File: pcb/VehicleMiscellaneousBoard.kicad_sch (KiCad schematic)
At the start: 4 parts, among them J1 Conn_02x05_Top_Bottom, U1 OpenMV H7+, U2 Seeed_Studio_XIAO-ESP32-S3-Se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

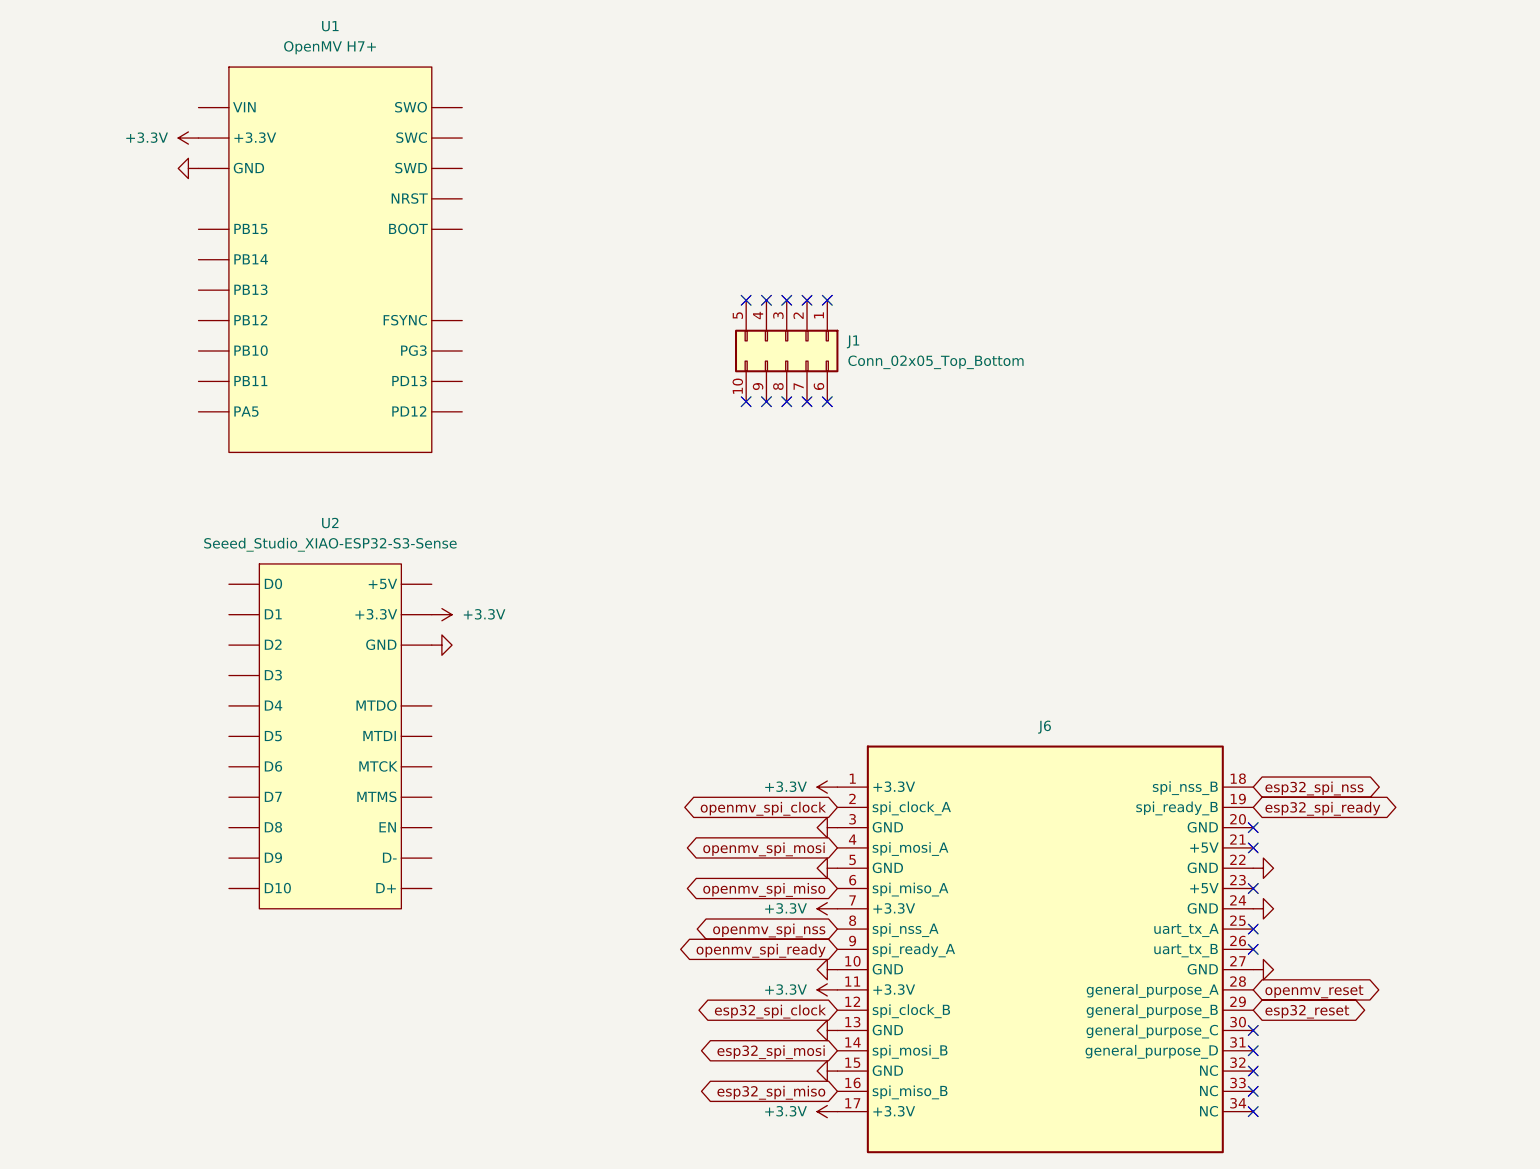
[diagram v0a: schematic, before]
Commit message: Routed `VehicleMiscellaneousBoard`.
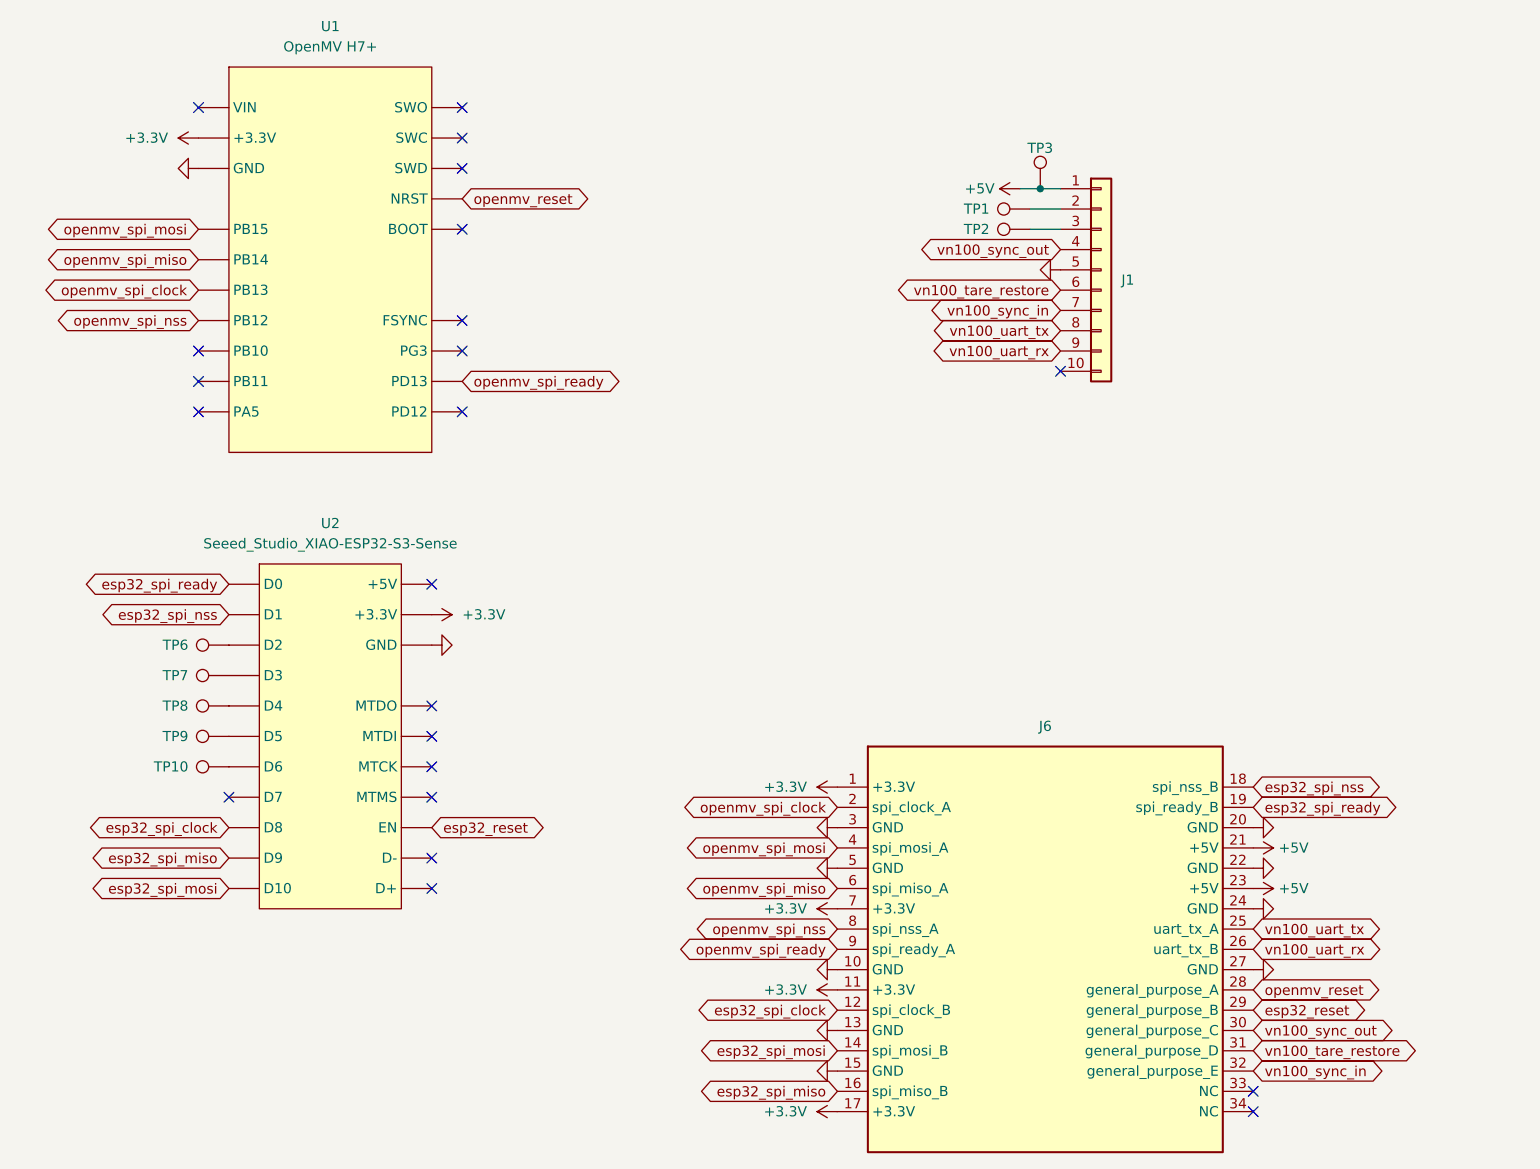
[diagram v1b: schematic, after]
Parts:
- added TP1, TP10, TP2, TP3, TP6, TP7, TP8, TP9: TestPoint, TestPoint:TestPoint_Pad_1.0x1.0mm, symbol Connector:TestPoint
- J1: symbol Connector_Generic:Conn_02x05_Top_Bottom -> Connector_Generic:Conn_01x10
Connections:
- net GND: now also J1.5 (Pin_5), J6.20 (GND)
- net esp32_reset: now also U2.EN
- net esp32_spi_clock: now also U2.D8
- net esp32_spi_miso: now also U2.D9
- net esp32_spi_mosi: now also U2.D10
- net esp32_spi_nss: now also U2.D1
- net esp32_spi_ready: now also U2.D0
- net openmv_reset: now also U1.NRST
- net openmv_spi_clock: now also U1.PB13
- net openmv_spi_miso: now also U1.PB14
- net openmv_spi_mosi: now also U1.PB15
- net openmv_spi_nss: now also U1.PB12
- net openmv_spi_ready: now also U1.PD13
- net +5V: now reaches J6.21 (+5V)
- net +5V: now also J1.1 (Pin_1), J6.23 (+5V), TP3.1
- net vn100_uart_tx: now reaches J6.25 (uart_tx_A)
- net vn100_uart_tx: now also J1.8 (Pin_8)
- net vn100_uart_rx: now reaches J6.26 (uart_tx_B)
- net vn100_uart_rx: now also J1.9 (Pin_9)
- net vn100_sync_out: now reaches J6.30 (general_purpose_C)
- net vn100_sync_out: now also J1.4 (Pin_4)
- net vn100_tare_restore: now reaches J6.31 (general_purpose_D)
- net vn100_tare_restore: now also J1.6 (Pin_6)
- net vn100_sync_in: now reaches J6.32 (general_purpose_E)
- net vn100_sync_in: now also J1.7 (Pin_7)
- net at U2.D2: now also TP6.1
- net at U2.D3: now also TP7.1
- net at U2.D4: now also TP8.1
- net at U2.D5: now also TP9.1
- net at U2.D6: now also TP10.1
- net at J1.2 (Pin_2): now also TP1.1
- net at J1.3 (Pin_3): now also TP2.1
- no-connect marks 20 -> 22
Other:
- moved on the sheet: J1

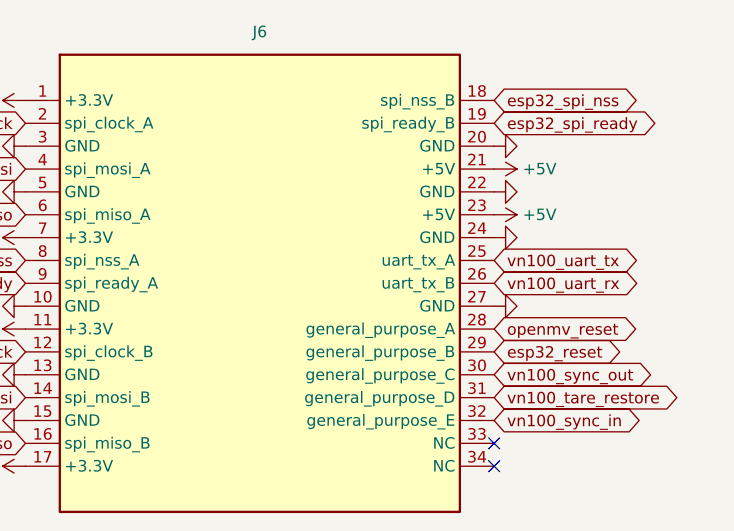
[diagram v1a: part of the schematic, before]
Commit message: Fixed inconsistency of `VehicleStackConnector` in `VehicleFlightComputer` and `VehicleMiscellaneousBoard`.
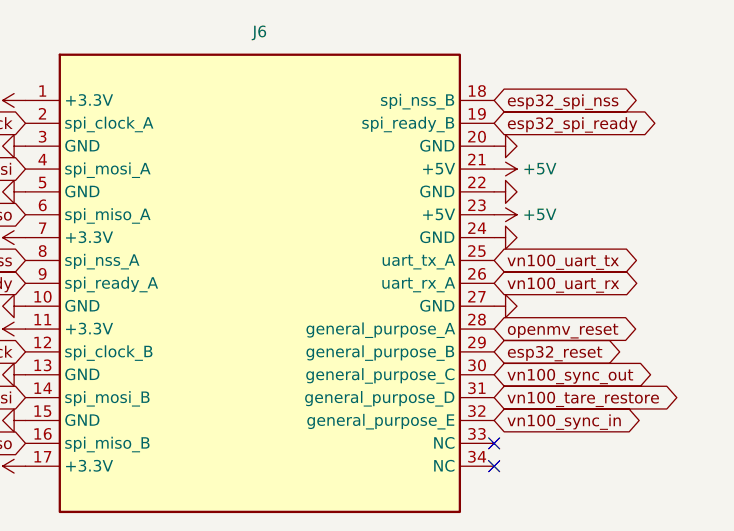
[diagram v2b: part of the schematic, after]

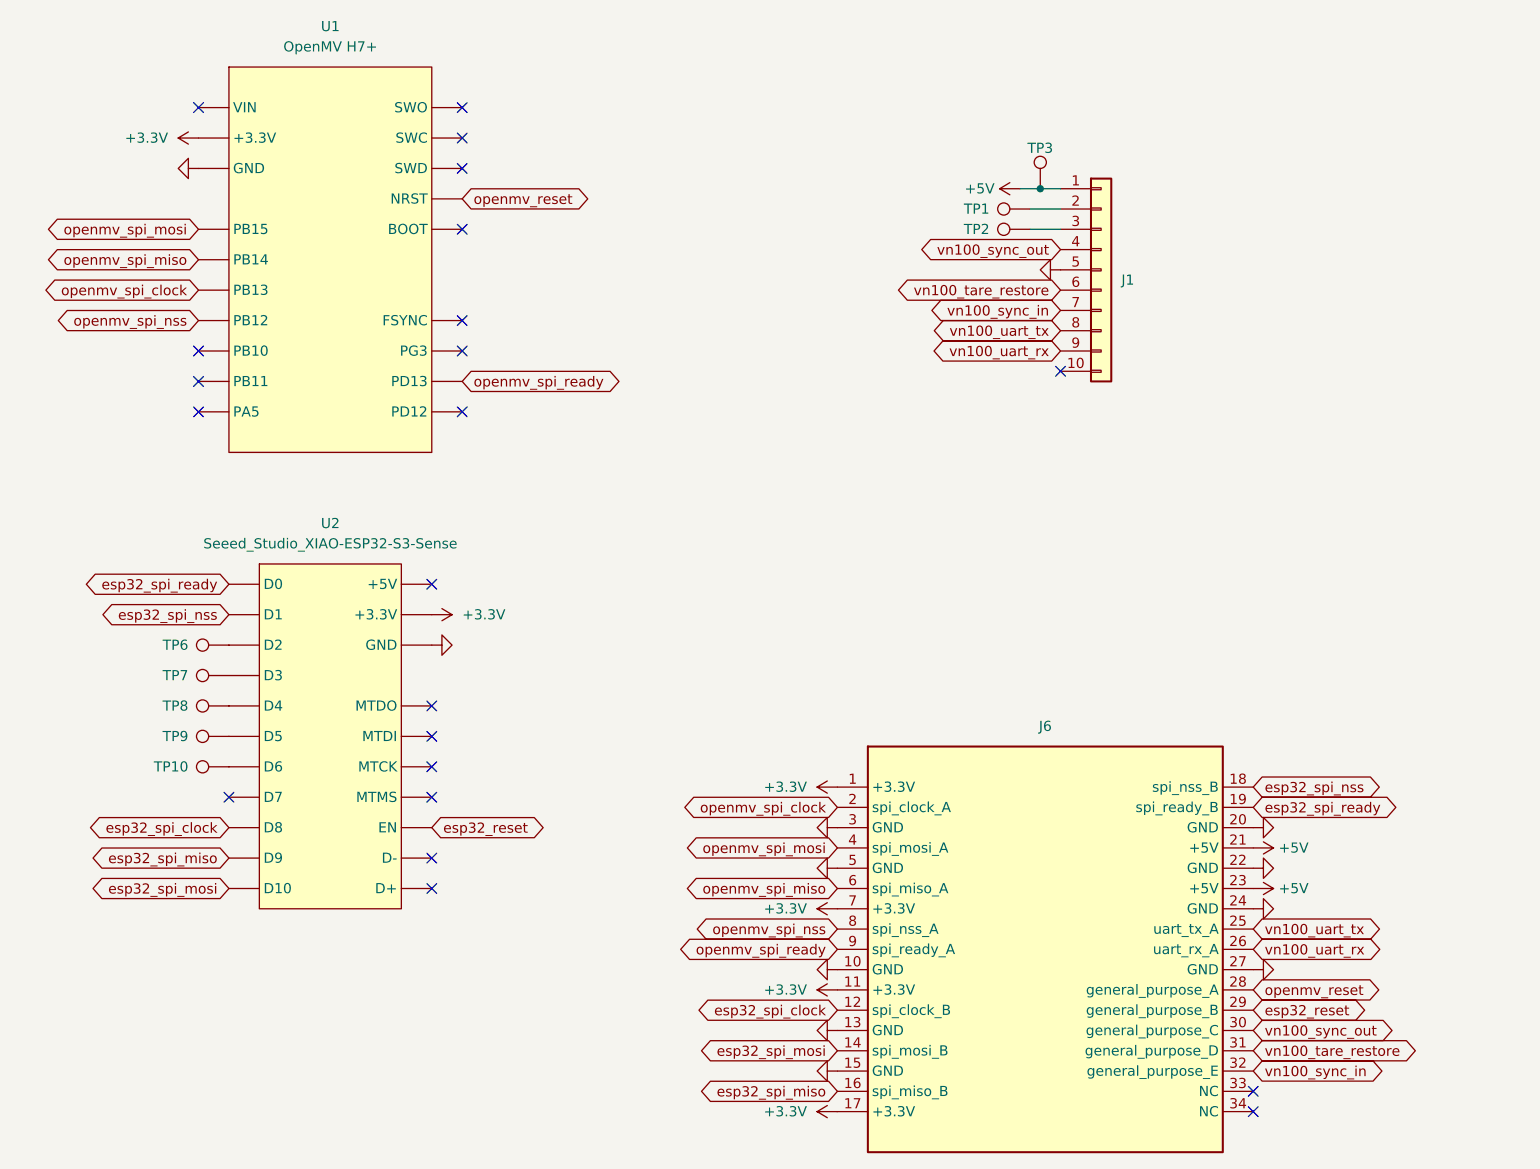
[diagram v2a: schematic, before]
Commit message: Made schematic symbol of vehicle stack connector match up with the footprint.
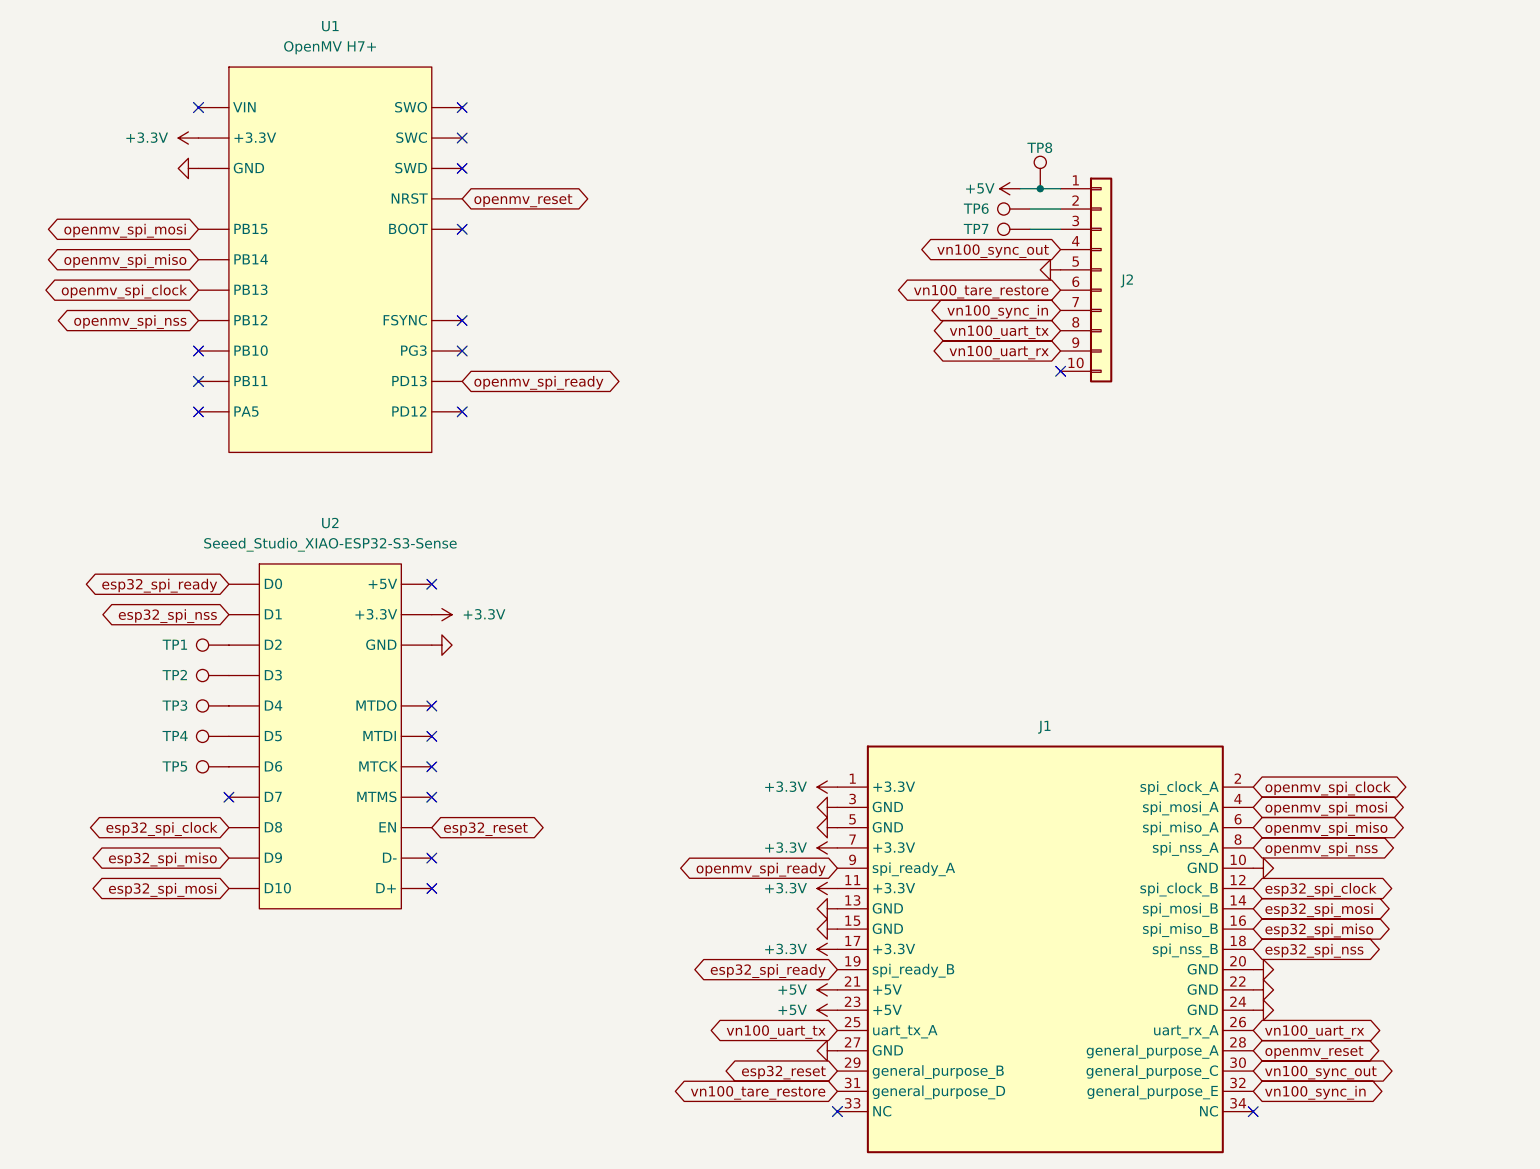
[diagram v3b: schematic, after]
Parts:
- renumbered J6 to J1, J1 to J2, TP6 to TP1, TP7 to TP2, TP8 to TP3, TP9 to TP4, TP10 to TP5, TP1 to TP6, TP2 to TP7, TP3 to TP8

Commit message: Errata fix `VFC-R1.1` and `VMISC-R1.1`: forgot to account for vehicle interface I2C bus.
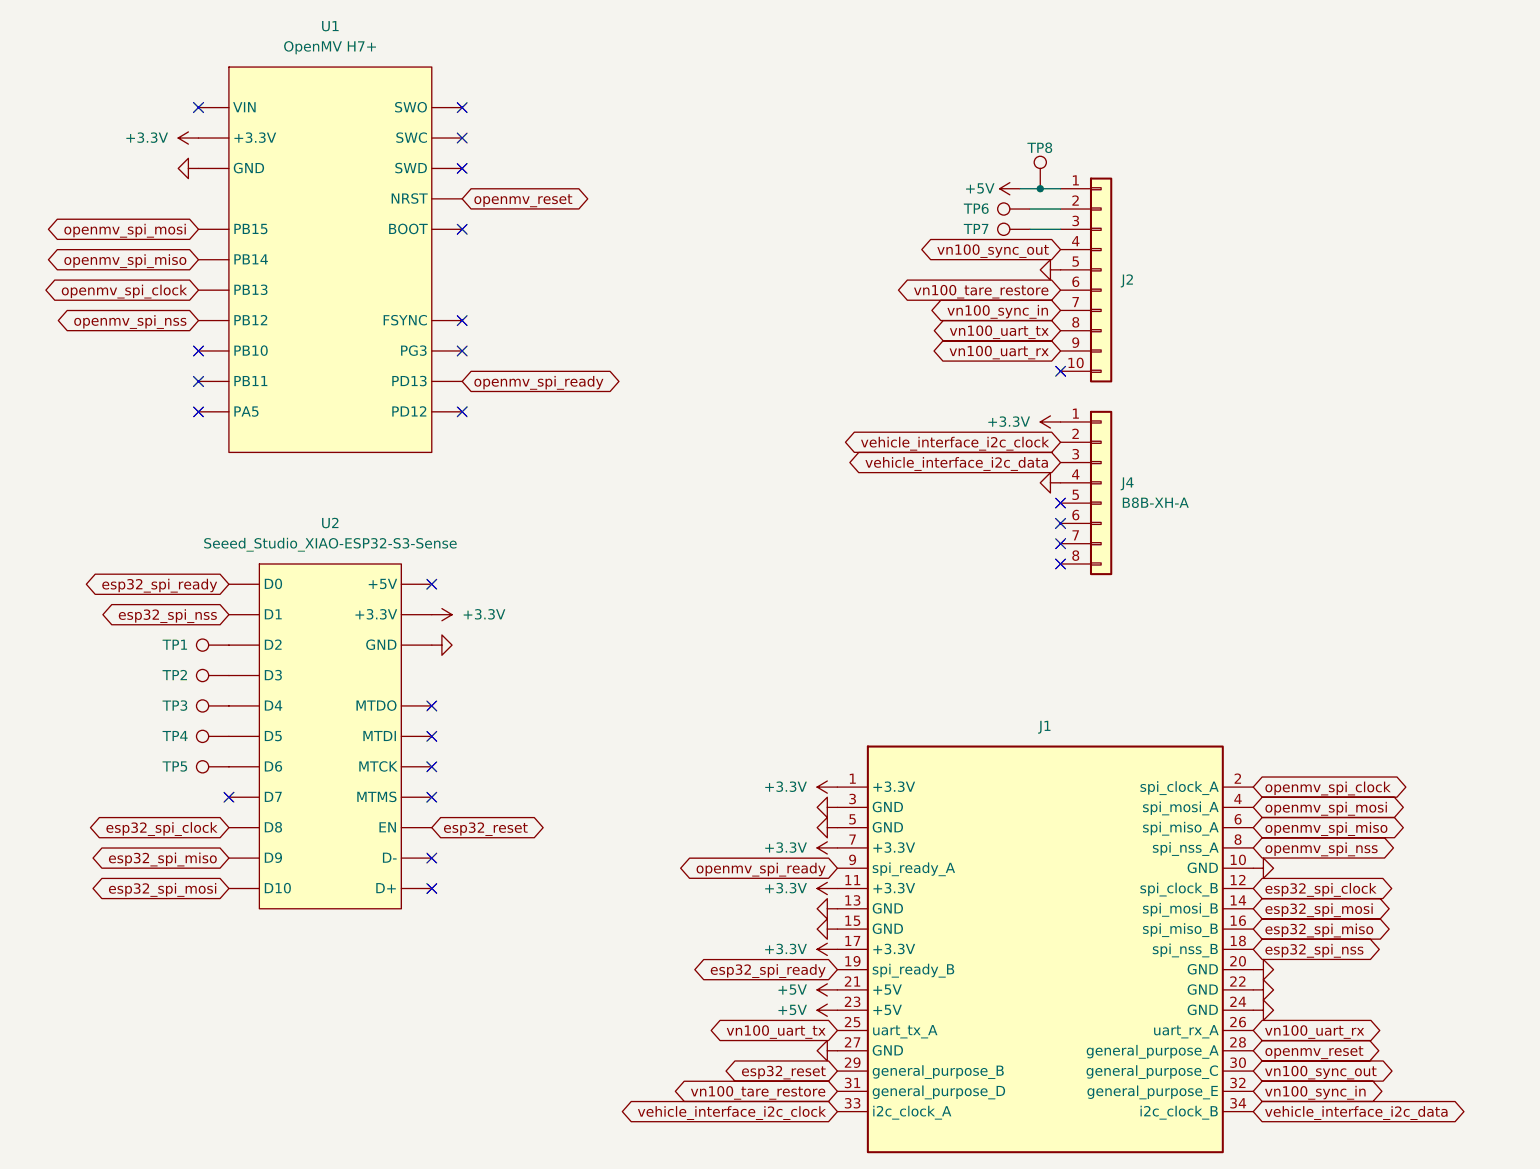
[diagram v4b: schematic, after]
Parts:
- added J4: B8B-XH-A, Connector_JST:JST_XH_B8B-XH-A_1x08_P2.50mm_Vertical, symbol Connector_Generic:Conn_01x08
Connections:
- net +3.3V: now also J4.1 (Pin_1)
- net GND: now also J4.4 (Pin_4)
- net vehicle_interface_i2c_clock: now reaches J1.33 (i2c_clock_A)
- net vehicle_interface_i2c_clock: now also J4.2 (Pin_2)
- net vehicle_interface_i2c_data: now reaches J1.34 (i2c_clock_B)
- net vehicle_interface_i2c_data: now also J4.3 (Pin_3)
- no-connect marks 22 -> 24
